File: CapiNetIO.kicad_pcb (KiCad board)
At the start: 2 copper layers, 58 parts, among them J1 USB_B_Micro, J2 SWD Prg, J4 USART3, J5 InterPCBBus1, J6 InterPCBBus2, SW1 SW_SPDT, U1 STM32F446RETx, U2 SN65HVD1781D, U3 AMS1117-3.3, U4 TLP290-4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

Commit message: checking components are present in pcb and renaming
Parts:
- removed LED1, LED2: 553-0122F, LED 553-0122F:5530122F
- added R17: 1k, Resistor_SMD:R_0402_1005Metric, F.Cu at (148.5, 110.5)
- added R18: 1k, Resistor_SMD:R_0402_1005Metric, F.Cu at (148.5, 112.5)
- added R19: 1k, Resistor_SMD:R_0402_1005Metric, F.Cu at (148.5, 114.5)
- added R20: 1k, Resistor_SMD:R_0402_1005Metric, F.Cu at (148.5, 116.5)
- added R3: 10K, Resistor_SMD:R_0402_1005Metric, F.Cu at (68.0, 59.0)
- added R4: 10K, Resistor_SMD:R_0402_1005Metric, F.Cu at (68.0, 61.0)
- added R5: 10K, Resistor_SMD:R_0402_1005Metric, F.Cu at (68.0, 63.0)
- added R6: 10K, Resistor_SMD:R_0402_1005Metric, F.Cu at (68.0, 65.0)
- added Status1: 553-0122F, LED 553-0122F:5530122F, F.Cu at (74.0, 40.0)
- added Status2: 553-0122F, LED 553-0122F:5530122F, F.Cu at (66.5, 40.0)
- moved R15 105.2 mm to (102.7, 137.2), turned to 90 degrees
- moved R16 102.5 mm to (104.7, 137.2), turned to 90 degrees
- moved R21 99.7 mm to (106.7, 137.2), turned to 90 degrees
- moved D6 97.1 mm to (107.0, 161.0), turned to 90 degrees
- moved R22 97.0 mm to (108.6, 137.2), turned to 90 degrees
- moved R23 94.2 mm to (110.6, 137.2), turned to 90 degrees
- moved R24 91.5 mm to (112.6, 137.2), turned to 90 degrees
- moved C14 88.9 mm to (114.4, 137.5), turned to 90 degrees
- moved C15 86.7 mm to (116.1, 137.5), turned to 90 degrees
- moved D7 82.2 mm to (117.7, 161.0), turned to 90 degrees
- moved SW1 46.8 mm to (56.5, 37.3)
- moved Outputs1 21.2 mm to (158.2, 71.2), turned to 90 degrees
- moved Inputs1 10.3 mm to (174.2, 120.2), turned to 90 degrees
- moved IN_Leds1 9.28 mm to (100.8, 40.0)
- moved Configuration1 8.01 mm to (60.0, 61.5), turned to -90 degrees
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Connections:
- net /485A renamed /485A+
- net /485B renamed /485B-

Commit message: Updating models
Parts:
- removed D1: LED, LED_SMD:LED_0603_1608Metric
- removed R1, R22, R23, R24, R3, R4, R5, R6: 10K, Resistor_SMD:R_0402_1005Metric
- removed R10, R2, R7, R8, R9: 1k5, Resistor_SMD:R_0402_1005Metric
- removed R19, R20: 1k, Resistor_SMD:R_0402_1005Metric
- removed U2: SN65HVD1781D, SN65HVD1781D:SN65HVD1781D
- removed U4, U5: TLP290-4, Package_SO:SOP-16_4.55x10.3mm_P1.27mm
- added 485trans1: SN65HVD1781D, SN65HVD1781D:SN65HVD1781D, F.Cu at (87.3, 115.1)
- added OptoIn1: TLP290-4, Package_SO:SOP-16_4.55x10.3mm_P1.27mm, F.Cu at (106.0, 55.5)
- added OptoOut1: TLP290-4, Package_SO:SOP-16_4.55x10.3mm_P1.27mm, F.Cu at (109.2, 89.6)
- added Power1: LED, LED_SMD:LED_0603_1608Metric, F.Cu at (80.8, 71.8)
- added R01: 10K, Resistor_SMD:R_0402_1005Metric, F.Cu at (60.0, 54.5)
- added R11: 1k5, Resistor_SMD:R_0402_1005Metric, F.Cu at (66.6, 57.5)
- added R12: 1k5, Resistor_SMD:R_0402_1005Metric, F.Cu at (66.6, 59.5)
- added R13: 1k5, Resistor_SMD:R_0402_1005Metric, F.Cu at (66.6, 61.5)
- added R14: 1k5, Resistor_SMD:R_0402_1005Metric, F.Cu at (66.6, 63.5)
- added R51: 10K, Resistor_SMD:R_0402_1005Metric, F.Cu at (69.5, 61.5)
- added R52: 10K, Resistor_SMD:R_0402_1005Metric, F.Cu at (69.5, 63.5)
- added R_35: 1k5, Resistor_SMD:R_0402_1005Metric, F.Cu at (83.1, 67.5)
- added R_36: 1k5, Resistor_SMD:R_0402_1005Metric, F.Cu at (83.1, 69.5)
- added R_37: 1k5, Resistor_SMD:R_0402_1005Metric, F.Cu at (86.0, 59.5)
- added R_38: 1k5, Resistor_SMD:R_0402_1005Metric, F.Cu at (86.0, 61.5)
- added R_41: 1k, Resistor_SMD:R_0402_1005Metric, F.Cu at (86.0, 63.5)
- added R_42: 1k, Resistor_SMD:R_0402_1005Metric, F.Cu at (86.0, 65.5)
- added R_43: 1k, Resistor_SMD:R_0402_1005Metric, F.Cu at (86.0, 67.5)
- added R_44: 1k, Resistor_SMD:R_0402_1005Metric, F.Cu at (86.0, 69.5)
- added R_45: 10K, Resistor_SMD:R_0402_1005Metric, F.Cu at (88.9, 59.5)
- added R_46: 10K, Resistor_SMD:R_0402_1005Metric, F.Cu at (88.9, 61.5)
- added R_47: 10K, Resistor_SMD:R_0402_1005Metric, F.Cu at (88.9, 63.5)
- added R_48: 10K, Resistor_SMD:R_0402_1005Metric, F.Cu at (88.9, 65.5)
- R17, R18: value 1k -> 10K
- R21: value 10K -> 1k5
- moved R17 102.3 mm to (62.9, 54.5)
- moved R18 96.3 mm to (69.5, 57.5)
- moved R21 86.1 mm to (69.5, 59.5), turned to 0 degrees
- moved Inputs1 56.3 mm to (155.2, 67.2)
- moved C14 54.6 mm to (65.0, 114.2)
- moved J1 54.1 mm to (52.5, 58.0)
- moved C15 52.6 mm to (69.0, 114.0)
- moved D6 50.6 mm to (148.8, 132.5)
- moved D7 50.6 mm to (159.5, 132.5)
- moved H1 41.0 mm to (188.0, 127.5)
- moved R15 37.6 mm to (73.0, 114.0)
- moved R16 36.1 mm to (77.0, 114.0)
- moved C12 22.1 mm to (128.5, 120.0)
- moved C13 22.1 mm to (120.5, 112.5)
- moved C5 22.1 mm to (133.0, 113.5)
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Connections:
- R15 pad 1: /USART2_RX -> Net-(Configuration1-NO_4)
- R15 pad 2: +3.3V -> /GPIO_in0
- R16 pad 1: GND -> Net-(Configuration1-NO_3)
- R16 pad 2: /USART2_DE -> /GPIO_in1
- R17 pad 1: Net-(Inputs1-Pad2) -> Net-(Configuration1-NO_2)
- R17 pad 2: /InLED_A0 -> /GPIO_in2
- R18 pad 1: Net-(Inputs1-Pad3) -> Net-(Configuration1-NO_1)
- R18 pad 2: /InLED_A1 -> /GPIO_in3
- R21 pad 1: /GPIO_INCon0 -> /pwr_led_k
- R21 pad 2: +3.3V -> GND

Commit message: Status and dipswitches, checked, working on inputs
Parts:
- added DZ0: BZX84Cxx, Package_TO_SOT_SMD:SOT-23, F.Cu at (135.1, 54.6)
- added DZ1: BZX84Cxx, Package_TO_SOT_SMD:SOT-23, F.Cu at (135.1, 59.1)
- added DZ3: BZX84Cxx, Package_TO_SOT_SMD:SOT-23, F.Cu at (135.1, 63.5)
- added DZ4: BZX84Cxx, Package_TO_SOT_SMD:SOT-23, F.Cu at (135.1, 68.0)
- R11, R12, R13, R14: value 1k5 -> 220
- R_41, R_42: value 1k -> 1.5k
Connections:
- Inputs1 pad 1: Net-(Inputs1-Pad1) -> /InLED_Opto3
- OptoIn1 pad 2: Net-(Inputs1-Pad1) -> /InLED_Opto3
- OptoIn1 pad 4: Net-(Inputs1-Pad1) -> /InLED_Opto3
- OptoIn1 pad 6: Net-(Inputs1-Pad1) -> /InLED_Opto3
- OptoIn1 pad 8: Net-(Inputs1-Pad1) -> /InLED_Opto3

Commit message: checked outputs for resistors and circuits
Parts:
- removed DZ0, DZ1, DZ3, DZ4: BZX84Cxx, Package_TO_SOT_SMD:SOT-23
- removed Out_LEDS1: 551-0207-004F, LED 551 0207 004F:5510207004F
- added D1: SS14, Diode_SMD:D_SMA, F.Cu at (143.5, 68.6)
- added D2: SS14, Diode_SMD:D_SMA, F.Cu at (143.5, 64.0)
- added D3: SS14, Diode_SMD:D_SMA, F.Cu at (143.5, 59.5)
- added D4: SS14, Diode_SMD:D_SMA, F.Cu at (143.5, 55.0)
- added LED_Outputs1: 551-0207-004F, LED 551 0207 004F:5510207004F, F.Cu at (88.2, 38.5)
- added Q1: MMBT2222A, Package_TO_SOT_SMD:SOT-23, F.Cu at (115.0, 99.4)
- added Q2: MMBT2222A, Package_TO_SOT_SMD:SOT-23, F.Cu at (115.0, 93.2)
- added Q3: MMBT2222A, Package_TO_SOT_SMD:SOT-23, F.Cu at (115.0, 84.0)
- added Q4: MMBT2222A, Package_TO_SOT_SMD:SOT-23, F.Cu at (116.5, 73.5)
- added Z1: BZX884-C5V1-QYL, BZX884-C5V1-QYL:BZX884C5V1QYL, F.Cu at (130.7, 69.0)
- added Z2: BZX884-C5V1-QYL, BZX884-C5V1-QYL:BZX884C5V1QYL, F.Cu at (130.8, 64.0)
- added Z3: BZX884-C5V1-QYL, BZX884-C5V1-QYL:BZX884C5V1QYL, F.Cu at (131.2, 59.7)
- added Z4: BZX884-C5V1-QYL, BZX884-C5V1-QYL:BZX884C5V1QYL, F.Cu at (131.0, 54.5)
- R_35, R_36, R_38: value 1k5 -> 4k7
- R_37: value 1k5 -> 4K7
- moved R_44 52.7 mm to (136.5, 54.5)
- moved R_41 51.3 mm to (137.0, 69.5)
- moved R_42 50.5 mm to (136.5, 65.0)
- moved R_43 50.4 mm to (136.0, 61.5)
- moved OptoIn1 9.39 mm to (114.5, 59.5)
- moved OptoOut1 4.75 mm to (104.5, 89.5)
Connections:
- Inputs1 pad 1: /InLED_Opto3 -> /InputComms
- Inputs1 pad 2: Net-(Inputs1-Pad2) -> Net-(D1-K)
- Inputs1 pad 3: Net-(Inputs1-Pad3) -> Net-(D2-K)
- Inputs1 pad 4: Net-(Inputs1-Pad4) -> Net-(D3-K)
- Inputs1 pad 5: Net-(Inputs1-Pad5) -> Net-(D4-K)
- OptoIn1 pad 2: /InLED_Opto3 -> /InputComms
- OptoIn1 pad 4: /InLED_Opto3 -> /InputComms
- OptoIn1 pad 6: /InLED_Opto3 -> /InputComms
- OptoIn1 pad 8: /InLED_Opto3 -> /InputComms
- OptoOut1 pad 10: /Coi3 -> VBUS
- OptoOut1 pad 11: GND -> Net-(OptoOut1-Pad11)
- OptoOut1 pad 12: /Coi2 -> VBUS
- OptoOut1 pad 13: GND -> Net-(OptoOut1-Pad13)
- OptoOut1 pad 14: /Coi1 -> VBUS
- OptoOut1 pad 15: GND -> Net-(OptoOut1-Pad15)
- OptoOut1 pad 16: /Coi0 -> VBUS
- OptoOut1 pad 9: GND -> Net-(OptoOut1-Pad9)
- RLY1 pad 3: /Coi0 -> /Coi1
- RLY1 pad 4: /Out0 -> /Out1
- RLY2 pad 3: /Coi1 -> /Coi0
- RLY2 pad 4: /Out1 -> /Out0
- R_35 pad 1: VBUS -> Net-(OptoOut1-Pad15)
- R_35 pad 2: /Coi0 -> Net-(Q1-B)
- R_36 pad 1: VBUS -> Net-(OptoOut1-Pad13)
- R_36 pad 2: /Coi1 -> Net-(Q2-B)
- R_37 pad 1: VBUS -> Net-(OptoOut1-Pad11)
- R_37 pad 2: /Coi2 -> Net-(Q3-B)
- R_38 pad 1: VBUS -> Net-(OptoOut1-Pad9)
- R_38 pad 2: /Coi3 -> Net-(Q4-B)
- R_41 pad 1: Net-(Inputs1-Pad2) -> Net-(D1-A)
- R_42 pad 1: Net-(Inputs1-Pad3) -> Net-(D2-A)
- R_43 pad 1: Net-(Inputs1-Pad4) -> Net-(D3-A)
- R_44 pad 1: Net-(Inputs1-Pad5) -> Net-(D4-A)

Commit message: updated inter PCB bus, added jumper power from USB
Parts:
- removed J6: InterPCBBus2, Connector_PinHeader_1.00mm:PinHeader_1x05_P1.00mm_Vertical
- added InterPCB_Bus1: Conn_02x05_Row_Letter_Last, Connector_PinHeader_2.54mm:PinHeader_2x05_P2.54mm_Vertical, F.Cu at (74.5, 121.3)
- added USBpwr1: Conn_01x02_Pin, Connector_JST:JST_VH_S2P-VH_1x02_P3.96mm_Horizontal, F.Cu at (51.0, 70.5)
- J5: value InterPCBBus1 -> SWD Prg; footprint Connector_PinHeader_1.00mm:PinHeader_1x05_P1.00mm_Vertical -> Connector_PinHeader_1.00mm:PinHeader_1x04_P1.00mm_Vertical
- moved J5 42.6 mm to (51.5, 117.0)
- moved Configuration1 8.81 mm to (69.5, 74.5)
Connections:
- J1 pad 1: VBUS -> unconnected-(J1-VBUS-Pad1)
- J5 pad 1: VBUS -> unconnected-(J5-Pin_1-Pad1)
- J5 pad 2: /485B- -> unconnected-(J5-Pin_2-Pad2)
- J5 pad 3: Net-(J5-Pin_3) -> unconnected-(J5-Pin_3-Pad3)
- J5 pad 4: /485A+ -> unconnected-(J5-Pin_4-Pad4)

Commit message: Overall Check, need to update the pbc constrains to pass checks
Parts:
- removed IN_Leds1: 551-0207-004F, LED 551 0207 004F:5510207004F
- removed InterPCB_Bus1: Conn_02x05_Row_Letter_Last, Connector_PinHeader_2.54mm:PinHeader_2x05_P2.54mm_Vertical
- removed USBpwr1: Conn_01x02_Pin, Connector_JST:JST_VH_S2P-VH_1x02_P3.96mm_Horizontal
- removed Z4: BZX884-C5V1-QYL, BZX884-C5V1-QYL:BZX884C5V1QYL
- added J3: 1963421, 1963421_2Poles:1963421, F.Cu at (78.0, 39.4)
- added JP1: JumperPWR, TestPoint:TestPoint_2Pads_Pitch2.54mm_Drill0.8mm, F.Cu at (47.0, 71.5)
- added LED_Outputs2: 551-0207-004F, LED 551 0207 004F:5510207004F, F.Cu at (123.6, 34.5)
- added R32: 390, Resistor_SMD:R_0402_1005Metric, F.Cu at (103.0, 87.0)
- added R33: 390, Resistor_SMD:R_0402_1005Metric, F.Cu at (103.0, 89.0)
- added R34: 390, Resistor_SMD:R_0402_1005Metric, F.Cu at (103.0, 91.0)
- added R_31: 390, Resistor_SMD:R_0402_1005Metric, F.Cu at (103.0, 85.0)
- added Z5: BZX884-C5V1-QYL, BZX884-C5V1-QYL:BZX884C5V1QYL, F.Cu at (131.5, 68.5)
- J2, J4: footprint Connector_PinHeader_1.00mm:PinHeader_1x04_P1.00mm_Vertical -> Connector_PinHeader_2.54mm:PinHeader_1x04_P2.54mm_Horizontal
- J5: value SWD Prg -> Conn_02x05_Counter_Clockwise; footprint Connector_PinHeader_1.00mm:PinHeader_1x04_P1.00mm_Vertical -> Connector_IDC:IDC-Header_2x05_P2.54mm_Vertical
- moved C12 96.7 mm to (64.5, 47.5)
- moved C13 96.7 mm to (56.5, 40.0)
- moved C5 96.7 mm to (69.0, 41.0)
- moved U3 96.7 mm to (57.0, 46.5)
- moved R_38 47.2 mm to (116.5, 97.5)
- moved J5 44.7 mm to (94.7, 128.5), turned to -90 degrees
- moved R_37 43.8 mm to (116.5, 91.0)
- moved R_36 36.6 mm to (116.5, 84.5)
- moved R_35 34.9 mm to (116.5, 77.5)
- moved R12 33.1 mm to (94.0, 41.0)
- moved R11 31.3 mm to (94.0, 42.5)
- moved R14 29.4 mm to (85.5, 41.0), turned to 180 degrees
- moved R13 26.8 mm to (85.5, 42.5), turned to 180 degrees
- moved Q4 25.5 mm to (121.4, 98.5)
- moved R_48 23.2 mm to (111.0, 58.5), turned to 180 degrees
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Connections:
- J1 pad 1: unconnected-(J1-VBUS-Pad1) -> Net-(J1-VBUS)
- J5 pad 1: unconnected-(J5-Pin_1-Pad1) -> VBUS
- J5 pad 2: unconnected-(J5-Pin_2-Pad2) -> /485B-
- J5 pad 3: unconnected-(J5-Pin_3-Pad3) -> GND
- J5 pad 4: unconnected-(J5-Pin_4-Pad4) -> /485A+
- Z1 pad 1: /InLED_A0 -> /InLED_A1
- Z2 pad 1: /InLED_A1 -> /InLED_A2
- Z3 pad 1: /InLED_A2 -> /InLED_A3

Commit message: Checked footprints and pcb constrains, time to start tracing
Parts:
- removed D7: 5KPxxCA, Diode_THT:D_P600_R-6_P20.00mm_Horizontal
- added D5: ESD5Zxx, Diode_SMD:D_SOD-523, F.Cu at (105.5, 130.7)
- C1, C10, C11, C14, C15, C2, C3, C4: footprint Capacitor_SMD:C_01005_0402Metric -> Capacitor_SMD:C_0603_1608Metric
- C6, C7, C8, C9: footprint Capacitor_SMD:C_0402_1005Metric -> Capacitor_SMD:C_0603_1608Metric
- D6: value 5KPxxCA -> ESD5Zxx; footprint Diode_THT:D_P600_R-6_P20.00mm_Horizontal -> Diode_SMD:D_SOD-523
- moved D6 37.4 mm to (111.5, 130.5)
- moved R32 13.7 mm to (112.6, 96.8)
- moved R33 13.7 mm to (112.6, 98.8)
- moved R34 13.7 mm to (112.6, 100.8)
- moved OptoOut1 13.7 mm to (119.1, 97.8)
- moved Outputs1 13.7 mm to (163.6, 101.0)
- moved Q1 13.7 mm to (131.1, 88.2)
- moved Q2 13.7 mm to (131.1, 95.2)
- moved Q3 13.7 mm to (131.1, 101.8)
- moved Q4 13.7 mm to (131.1, 108.3)
- moved RLY1 13.7 mm to (141.0, 95.2)
- moved RLY2 13.7 mm to (141.0, 88.8)
- moved RLY3 13.7 mm to (141.0, 101.8)
- moved RLY4 13.7 mm to (141.0, 108.0)
- moved R_31 13.7 mm to (112.6, 94.8)
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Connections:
- D6 pad 1: GND -> /485B-
- D6 pad 2: /485B- -> GND
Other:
- board outline added: 152.4 x 107.9 mm

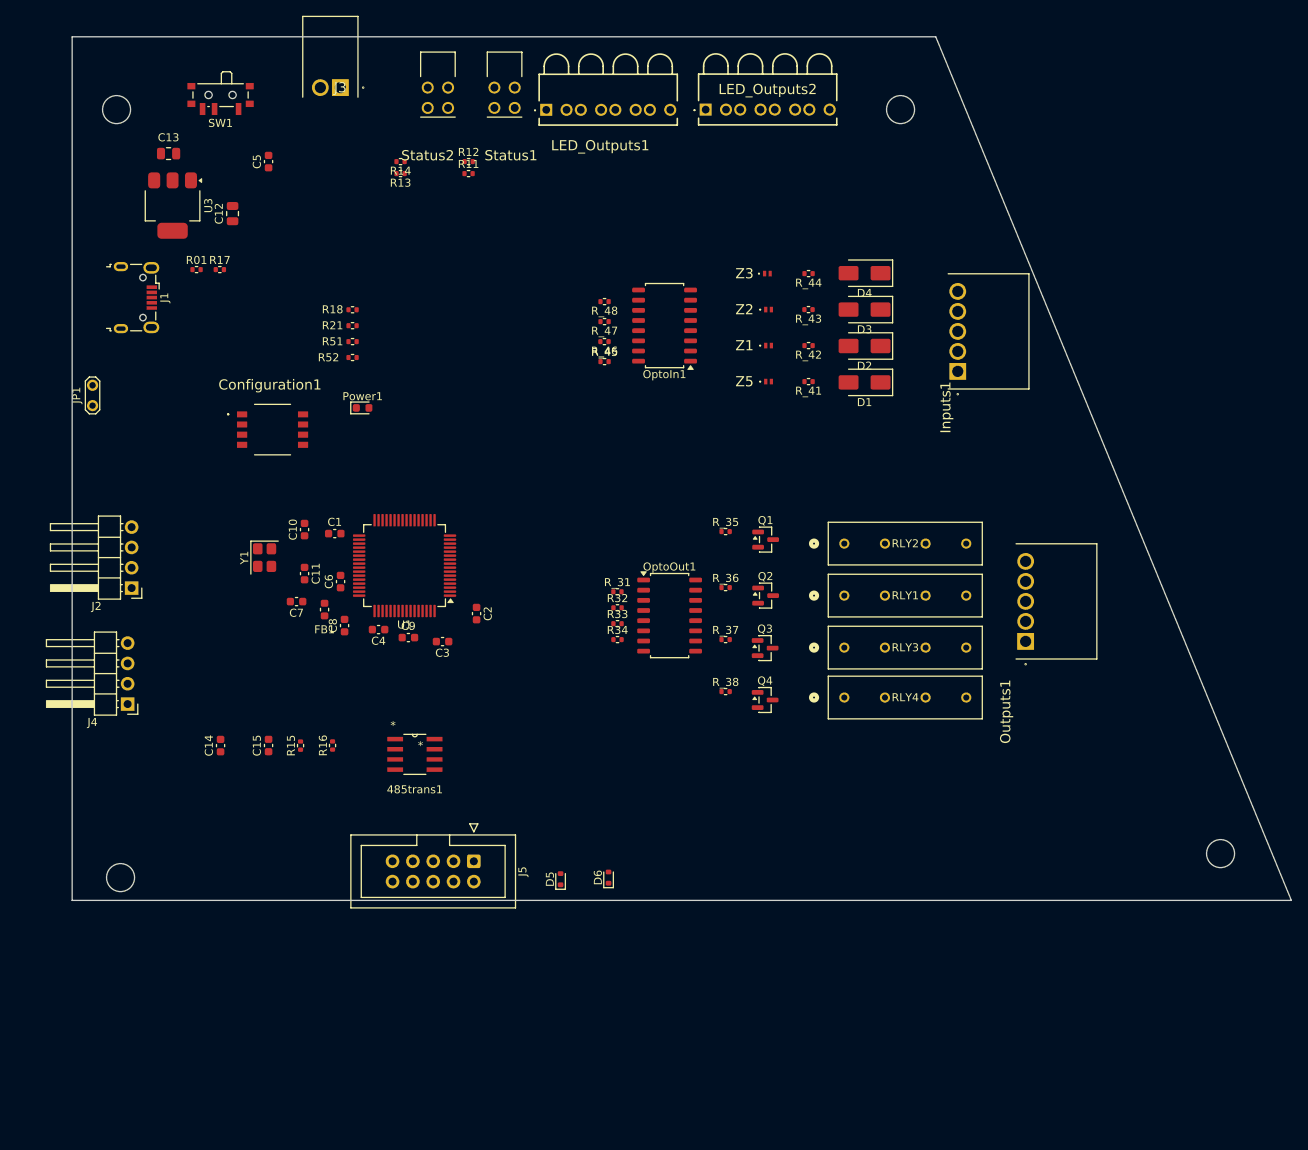
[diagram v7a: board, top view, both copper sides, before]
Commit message: Changed pins GPIO_Out0-3 and GPIO_In0-3 to a more accessible ones. Added project CubeMX
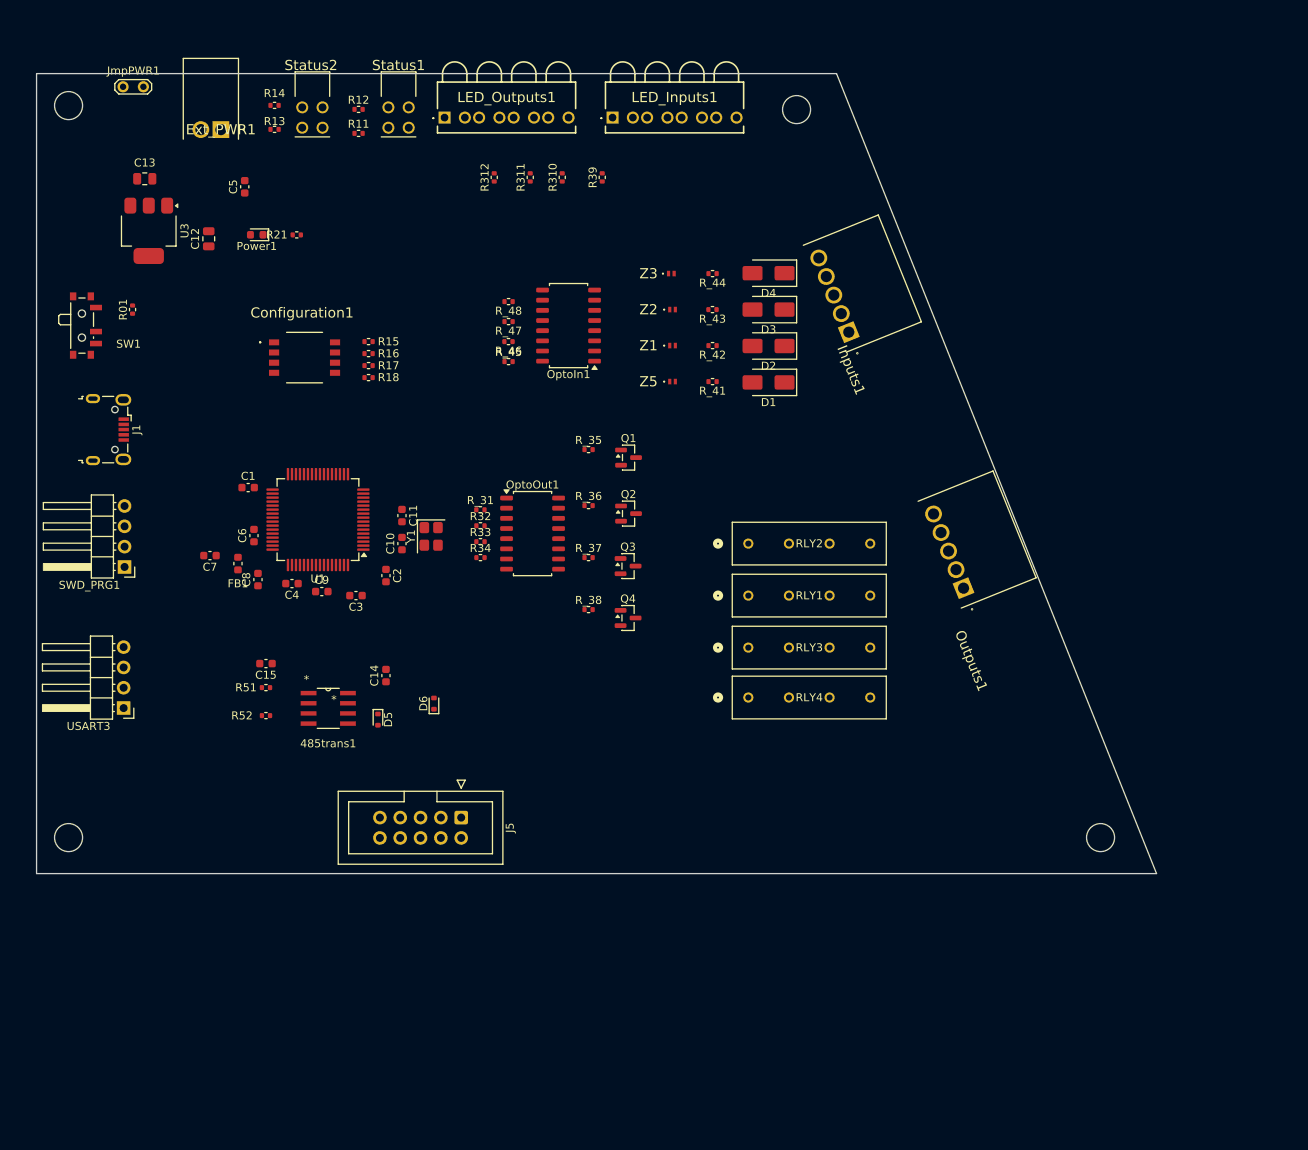
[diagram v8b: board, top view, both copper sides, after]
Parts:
- removed J2: SWD Prg, Connector_PinHeader_2.54mm:PinHeader_1x04_P2.54mm_Horizontal
- removed J3: 1963421, 1963421_2Poles:1963421
- removed J4: USART3, Connector_PinHeader_2.54mm:PinHeader_1x04_P2.54mm_Horizontal
- removed JP1: JumperPWR, TestPoint:TestPoint_2Pads_Pitch2.54mm_Drill0.8mm
- removed LED_Outputs2: 551-0207-004F, LED 551 0207 004F:5510207004F
- added Ext_PWR1: 1963421, 1963421_2Poles:1963421, F.Cu at (63.0, 37.0)
- added JmpPWR1: JumperPWR, TestPoint:TestPoint_2Pads_Pitch2.54mm_Drill0.8mm, F.Cu at (50.8, 31.6)
- added LED_Inputs1: 551-0207-004F, LED 551 0207 004F:5510207004F, F.Cu at (112.0, 35.5)
- added R310: 1k, Resistor_SMD:R_0402_1005Metric, F.Cu at (105.7, 43.0)
- added R311: 1k, Resistor_SMD:R_0402_1005Metric, F.Cu at (101.7, 43.0)
- added R312: 1k, Resistor_SMD:R_0402_1005Metric, F.Cu at (97.2, 43.0)
- added R39: 1k, Resistor_SMD:R_0402_1005Metric, F.Cu at (110.7, 43.0)
- added SWD_PRG1: SWD Prg, Connector_PinHeader_2.54mm:PinHeader_1x04_P2.54mm_Horizontal, F.Cu at (51.0, 91.7)
- added USART3: USART3, Connector_PinHeader_2.54mm:PinHeader_1x04_P2.54mm_Horizontal, F.Cu at (50.9, 109.3)
- moved R15 51.2 mm to (81.5, 63.5), turned to 0 degrees
- moved R16 49.2 mm to (81.5, 65.0), turned to 0 degrees
- moved R52 46.1 mm to (68.7, 110.2)
- moved R51 44.6 mm to (68.7, 106.8)
- moved SW1 33.2 mm to (46.0, 61.5), turned to -90 degrees
- moved D6 30.8 mm to (89.7, 108.8)
- moved D5 30.3 mm to (82.7, 110.8), turned to -90 degrees
- moved Power1 25.4 mm to (67.5, 50.1), turned to 180 degrees
- moved C14 22.5 mm to (83.7, 105.2)
- moved R17 22.1 mm to (81.5, 66.5)
- moved Y1 21.0 mm to (89.3, 87.8)
- moved R32 20.0 mm to (95.5, 86.5)
- moved R33 20.0 mm to (95.5, 88.5)
- moved R34 20.0 mm to (95.5, 90.5)
- moved OptoOut1 20.0 mm to (102.0, 87.5)
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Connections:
- net Net-(Configuration1-NO_1) renamed /Config3
- net Net-(Configuration1-NO_2) renamed /Config2
- net Net-(Configuration1-NO_3) renamed /Config1
- net Net-(Configuration1-NO_4) renamed /Config0
- OptoIn1 pad 10: /GPIO_INCon4 -> /GPIO_in3
- OptoIn1 pad 12: /GPIO_INCon2 -> /GPIO_in2
- OptoIn1 pad 14: /GPIO_INCon1 -> /GPIO_in1
- OptoIn1 pad 16: /GPIO_INCon0 -> /GPIO_in0
- R15 pad 2: /GPIO_in0 -> /GPIO_INCon0
- R16 pad 2: /GPIO_in1 -> /GPIO_INCon1
- R17 pad 2: /GPIO_in2 -> /GPIO_INCon2
- R18 pad 2: /GPIO_in3 -> /GPIO_INCon3
- R_45 pad 1: /GPIO_INCon0 -> /GPIO_in0
- R_46 pad 1: /GPIO_INCon1 -> /GPIO_in1
- R_47 pad 1: /GPIO_INCon2 -> /GPIO_in2
- R_48 pad 1: /GPIO_INCon4 -> /GPIO_in3
- U1 pad 24: unconnected-(U1-PC4-Pad24) -> /GPIO_out1
- U1 pad 26: unconnected-(U1-PB0-Pad26) -> /GPIO_out2
- U1 pad 27: unconnected-(U1-PB1-Pad27) -> /GPIO_out3
- U1 pad 28: unconnected-(U1-PB2-Pad28) -> /GPIO_out0
- U1 pad 34: /GPIO_INCon2 -> /GPIO_INCon1
- U1 pad 35: /GPIO_INCon3 -> /GPIO_INCon2
- U1 pad 55: /GPIO_out0 -> unconnected-(U1-PB3-Pad55)
- U1 pad 56: /GPIO_out1 -> unconnected-(U1-PB4-Pad56)
- U1 pad 57: /GPIO_out2 -> unconnected-(U1-PB5-Pad57)
- U1 pad 58: /GPIO_out3 -> unconnected-(U1-PB6-Pad58)
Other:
- board size 152.4 x 107.9 mm -> 140 x 100 mm
